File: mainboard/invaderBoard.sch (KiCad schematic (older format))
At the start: 27 parts, among them J1 Conn_01x02, J10 Conn_01x03, J11 Conn_01x04, J13 Conn_01x03, J19 Conn_01x02, J2 USB_A, J20 Conn_01x02, J3 Conn_01x04, J4 Conn_02x04_Odd_Even, J5 Conn_02x04_Odd_Even, J6 Conn_01x03, J7 Conn_01x03, J8 Conn_01x03, Q1 IRFZ44, SW1 SW_DIP_x01, U1 LM2596, U3 ArduinoMicro

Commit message: PCB holes added + capacitor simulator in LTspice
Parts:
- added H1, H2, H3: MountingHole, MountingHole:MountingHole_3.2mm_M3, symbol Mechanical:MountingHole
- U1: symbol bluerSaab:LM2596 -> invaderBoard-rescue:LM2596-bluerSaab
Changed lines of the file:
@@
 	2650 3900 2650 2400
 $Comp
-L bluerSaab:LM2596 U1
+L invaderBoard-rescue:LM2596-bluerSaab U1
 U 1 1 5D36BBF8
 P 6600 1200
@@
 NoConn ~ 2350 6400
 NoConn ~ 2350 6500
+$Comp
+L Mechanical:MountingHole H1
+U 1 1 5D483510
+P 7750 3750
+F 0 "H1" H 7850 3796 50  0000 L CNN
+F 1 "MountingHole" H 7850 3705 50  0000 L CNN
+F 2 "MountingHole:MountingHole_3.2mm_M3" H 7750 3750 50  0001 C CNN
+F 3 "~" H 7750 3750 50  0001 C CNN
+	1    7750 3750
+	1    0    0    -1
+$EndComp
+$Comp
+L Mechanical:MountingHole H2
+U 1 1 5D48397E
+P 7750 4000
+F 0 "H2" H 7850 4046 50  0000 L CNN
+F 1 "MountingHole" H 7850 3955 50  0000 L CNN
+F 2 "MountingHole:MountingHole_3.2mm_M3" H 7750 4000 50  0001 C CNN
+F 3 "~" H 7750 4000 50  0001 C CNN
+	1    7750 4000
+	1    0    0    -1
+$EndComp
+$Comp
+L Mechanical:MountingHole H3
+U 1 1 5D483CFA
+P 7750 4250
+F 0 "H3" H 7850 4296 50  0000 L CNN
+F 1 "MountingHole" H 7850 4205 50  0000 L CNN
+F 2 "MountingHole:MountingHole_3.2mm_M3" H 7750 4250 50  0001 C CNN
+F 3 "~" H 7750 4250 50  0001 C CNN
+	1    7750 4250
+	1    0    0    -1
+$EndComp
 $EndSCHEMATC

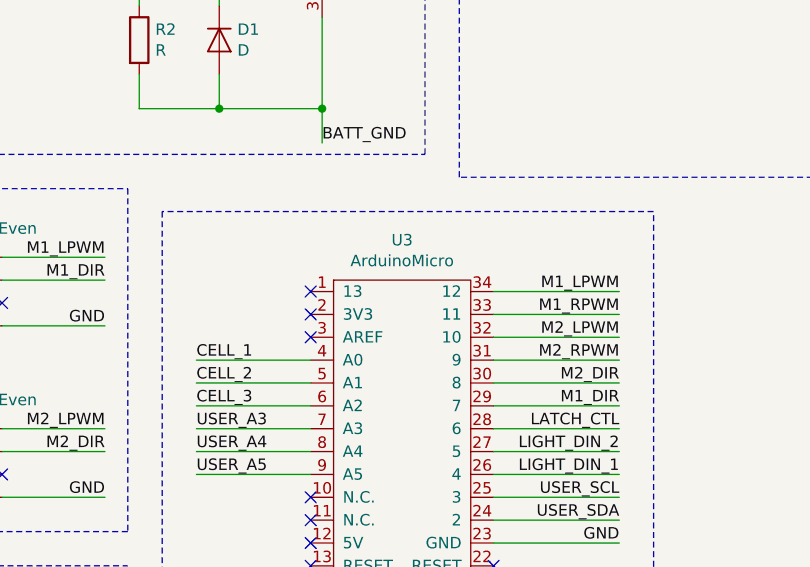
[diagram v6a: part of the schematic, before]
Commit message: arduino FW added + some changes on sch.
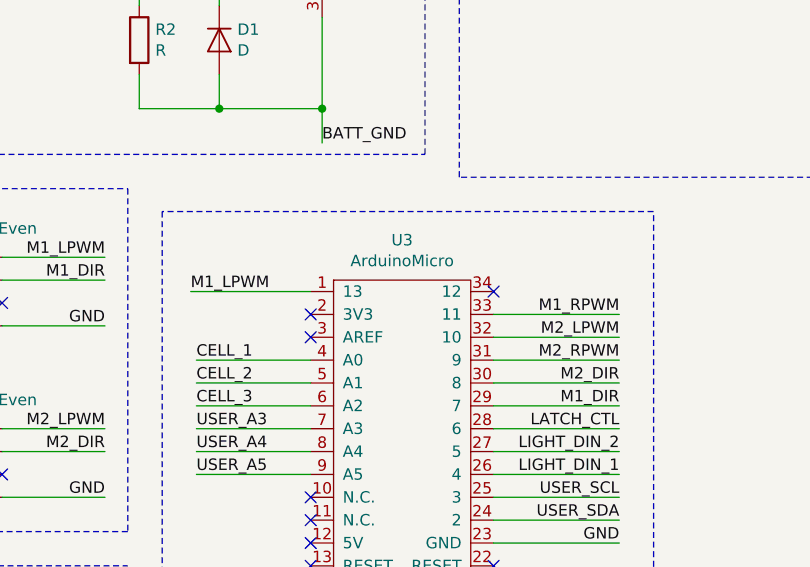
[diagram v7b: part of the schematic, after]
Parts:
- J1: footprint Connector_Wire:SolderWirePad_1x02_P7.62mm_Drill2mm -> .pretty:BiggerSolderPad
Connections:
- net M1_LPWM: now also U3.1 (13); no longer U3.34 (12)
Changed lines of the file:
@@
 F 0 "J1" H 818 1267 50  0000 C CNN
 F 1 "Conn_01x02" H 818 1176 50  0000 C CNN
-F 2 "Connector_Wire:SolderWirePad_1x02_P7.62mm_Drill2mm" H 900 1050 50  0001 C CNN
+F 2 ".pretty:BiggerSolderPad" H 900 1050 50  0001 C CNN
 F 3 "~" H 900 1050 50  0001 C CNN
 	1    900  1050
@@
 	1    0    0    -1
 $EndComp
-NoConn ~ 5050 2850
 NoConn ~ 5050 2950
 NoConn ~ 5050 3050
@@
 Text Label 6400 2950 2    50   ~ 0
 M1_RPWM
-Text Label 6400 2850 2    50   ~ 0
+Text Label 4525 2850 0    50   ~ 0
 M1_LPWM
 Wire Wire Line
-	6400 2850 5850 2850
+	4525 2850 5050 2850
 Wire Wire Line
 	5850 2950 6400 2950
@@
 	1    0    0    -1
 $EndComp
+NoConn ~ 5850 2850
 $EndSCHEMATC
